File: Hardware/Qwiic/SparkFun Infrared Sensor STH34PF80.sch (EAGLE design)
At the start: 26 parts, among them J1 Vertical Qwiic Connector, J2 Vertical Qwiic Connector

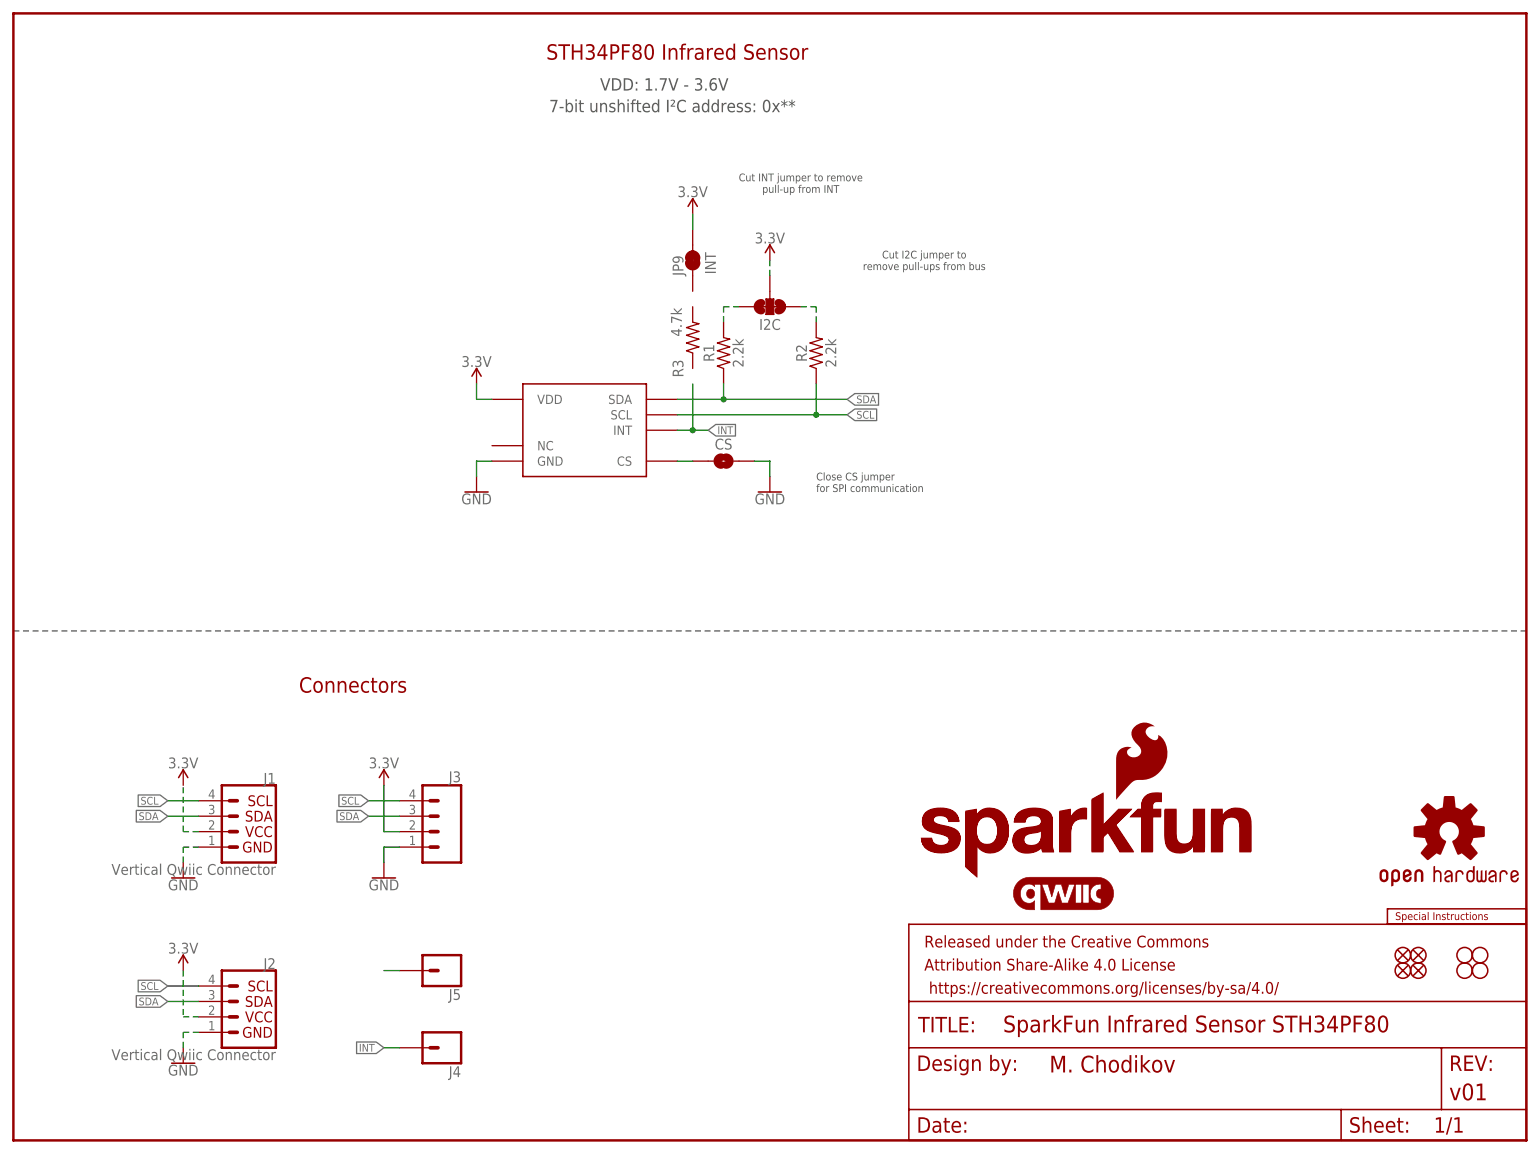
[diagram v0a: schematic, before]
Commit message: Continued design
Adjusted symbol and footprint to reflect the I2C AND SPI interfaces. Uploading to change name in GitHub for official product name
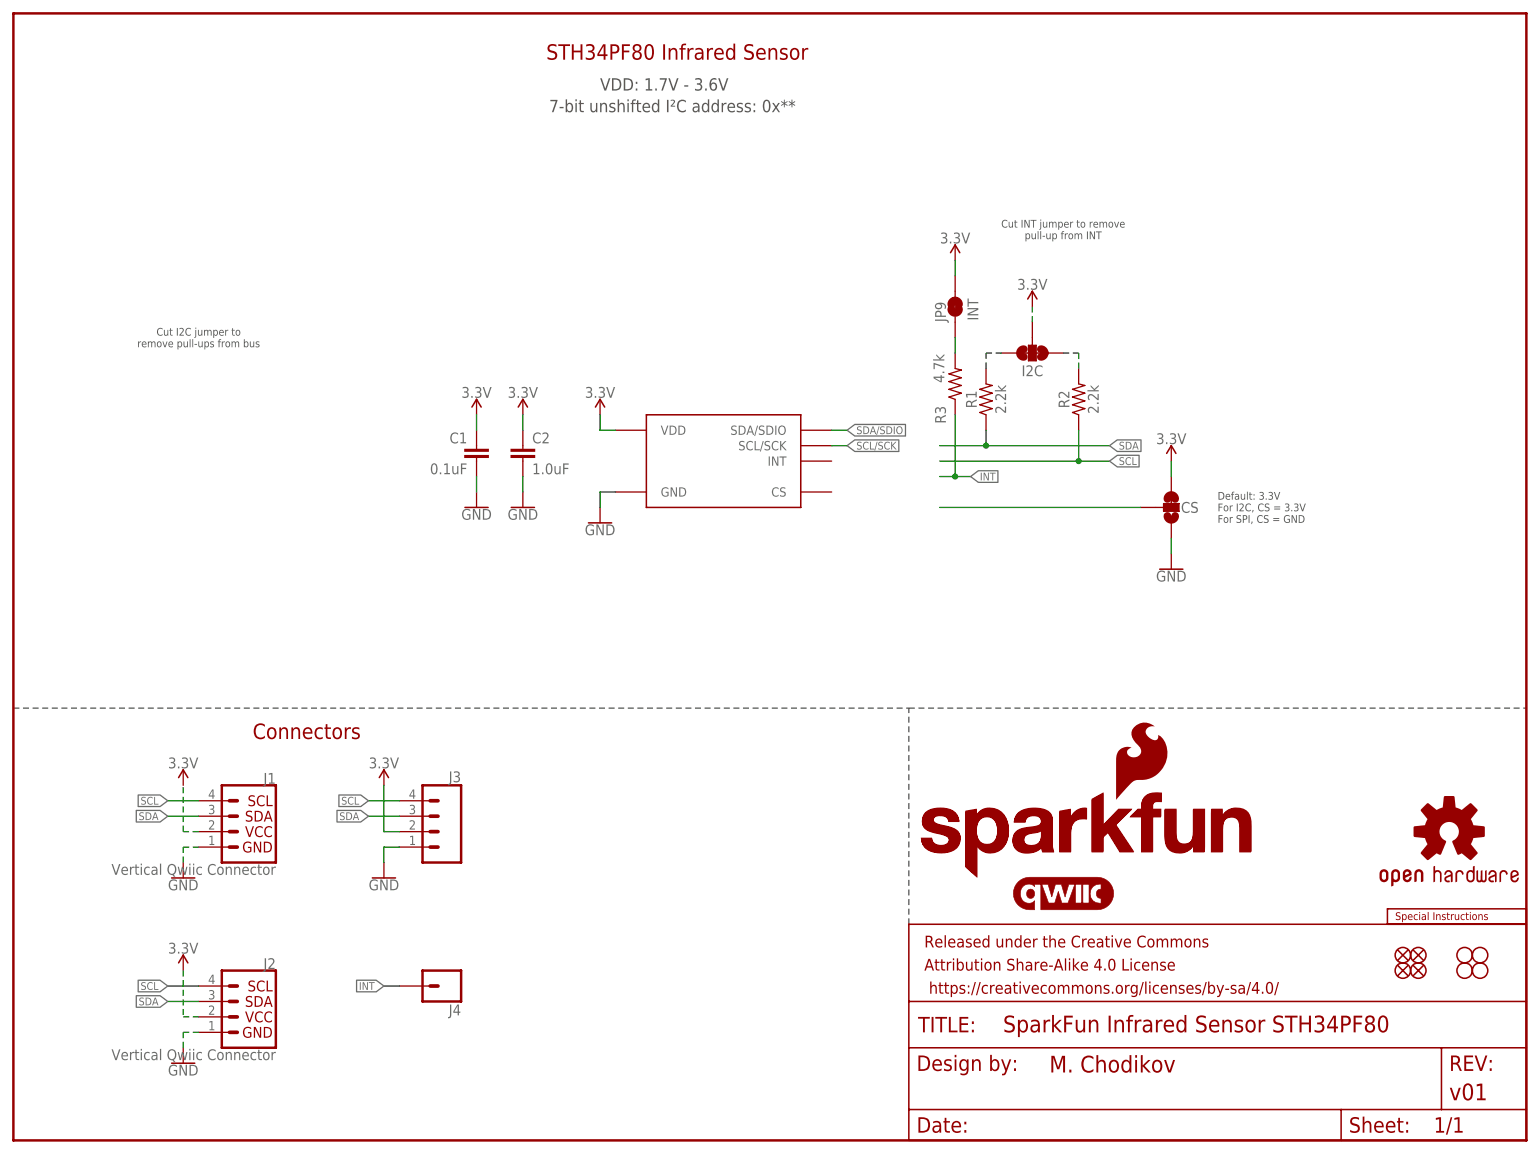
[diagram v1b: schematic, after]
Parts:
- removed J5: (no value), SparkFun-Connectors:CONN_01PTH_NO_SILK_YES_STOP
- added C1: 0.1uF, SparkFun-Capacitors:0.1UF-0603-25V-10%-X7R-WE
- added C2: 1.0uF, SparkFun-Capacitors:1.0UF-0603-16V-10%-X7R
- CS: value JUMPER-SMT_2_NO_SILK -> JUMPER-SMT_3_1-NC_TRACE_SILK; device SparkFun-Jumpers:JUMPER-SMT_2_NO_SILK -> SparkFun-Jumpers:JUMPER-SMT_3_1-NC_TRACE_SILK
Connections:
- new net SCL/SCK: U$1.SCL/SCK
- new net SDA/SDIO: U$1.SDA/SDIO
- net 3.3V: now also C1.1, C2.1, CS.3
- net GND: now also C1.2, C2.2, CS.1; no longer CS.2
- net INT: now also R3.1; no longer U$1.INT
- net N$3: now also CS.2; no longer CS.1, U$1.CS
- net N$4: now also JP9.1, R3.2; no longer J5.1
- net SCL: no longer U$1.SCL
- net SDA: no longer U$1.SDA
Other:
- note added: "Default: 3.3V For I2C, CS = 3.3V For SPI, CS = GND"
- note removed: "Close CS jumper for SPI communication"
- moved on the sheet: I2C, J4, JP9, R1, R2, R3

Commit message: Updates to Mini - uploading to change repo name
Continued mini board design
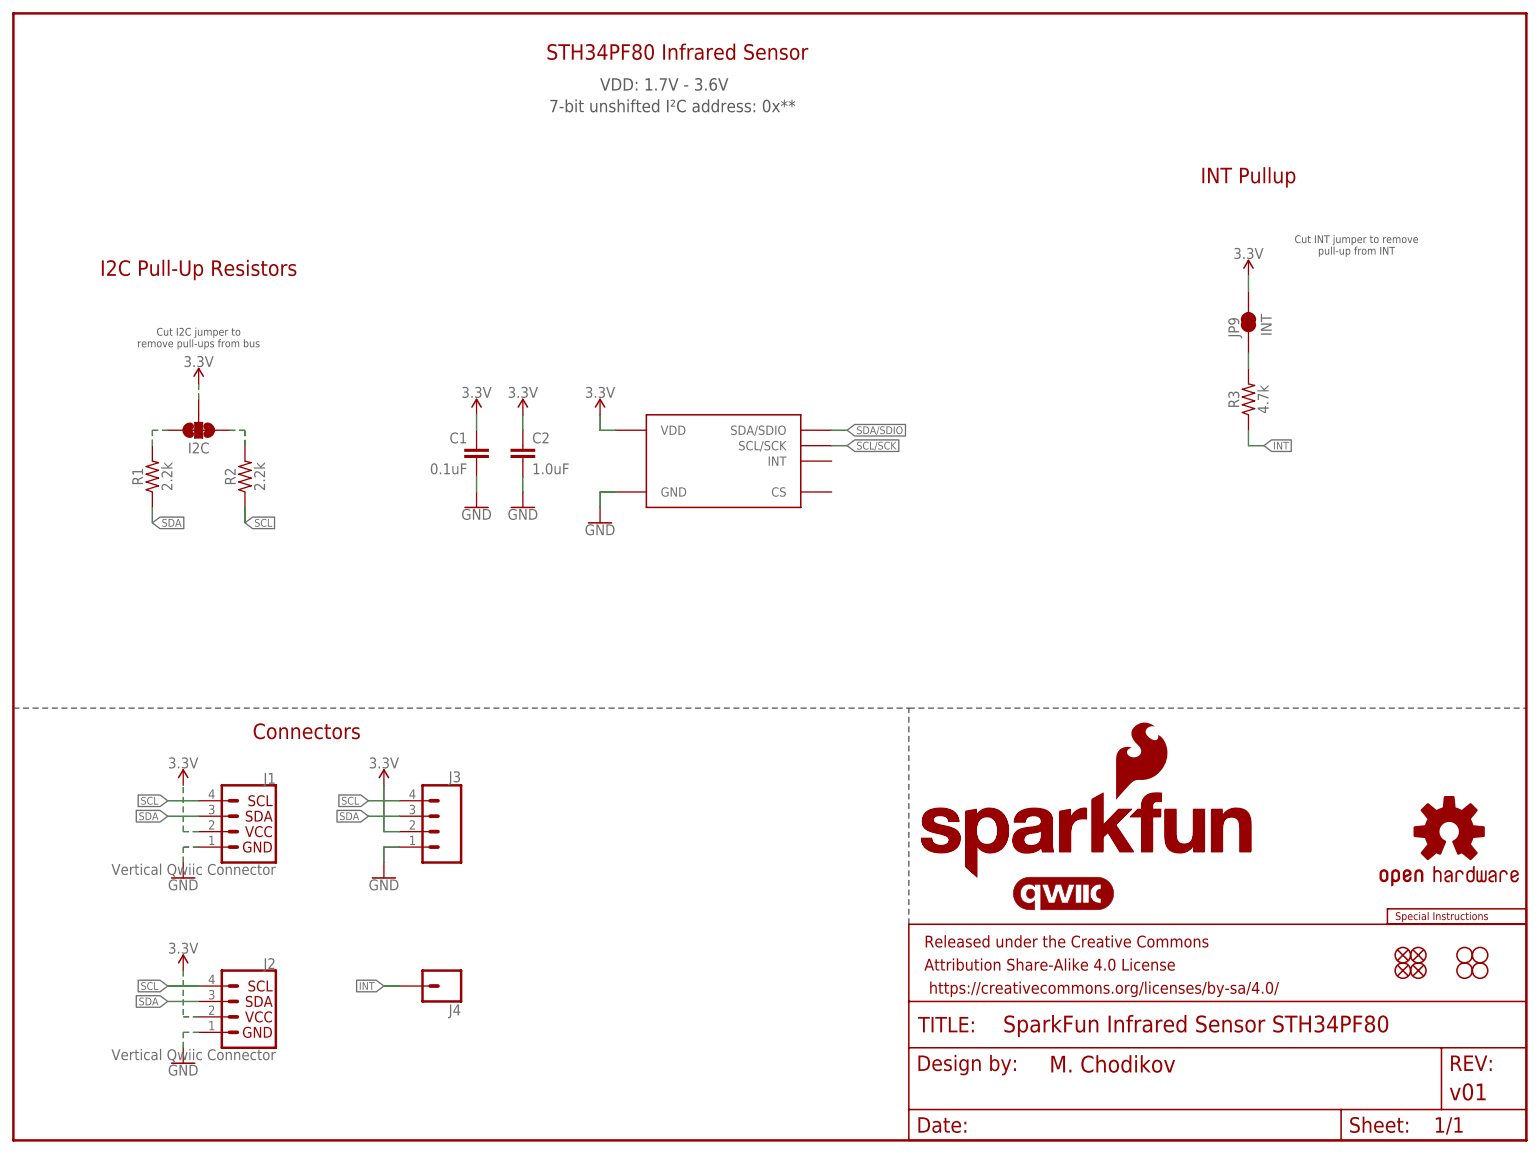
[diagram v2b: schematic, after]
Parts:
- removed CS: JUMPER-SMT_3_1-NC_TRACE_SILK, SparkFun-Jumpers:JUMPER-SMT_3_1-NC_TRACE_SILK
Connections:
- removed net N$3: CS.2
- net 3.3V: no longer CS.3
- net GND: no longer CS.1
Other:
- note added: "I2C Pull-Up Resistors"
- note added: "INT Pullup"
- note removed: "Default: 3.3V For I2C, CS = 3.3V For SPI, CS = GND"
- moved on the sheet: I2C, JP9, R1, R2, R3
